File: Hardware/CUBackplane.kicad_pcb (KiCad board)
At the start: 2 copper layers, 84.6 x 83.8 mm, 50 parts, among them CON1 EXPANSION BUS, CON2 EXPANSION BUS, CON3 EXPANSION BUS, CON4 EXPANSION BUS, J1 +5V, J2 -12V, J3 +12V, J4 -5V, J5 +15V, J6 -15V, J7 GND

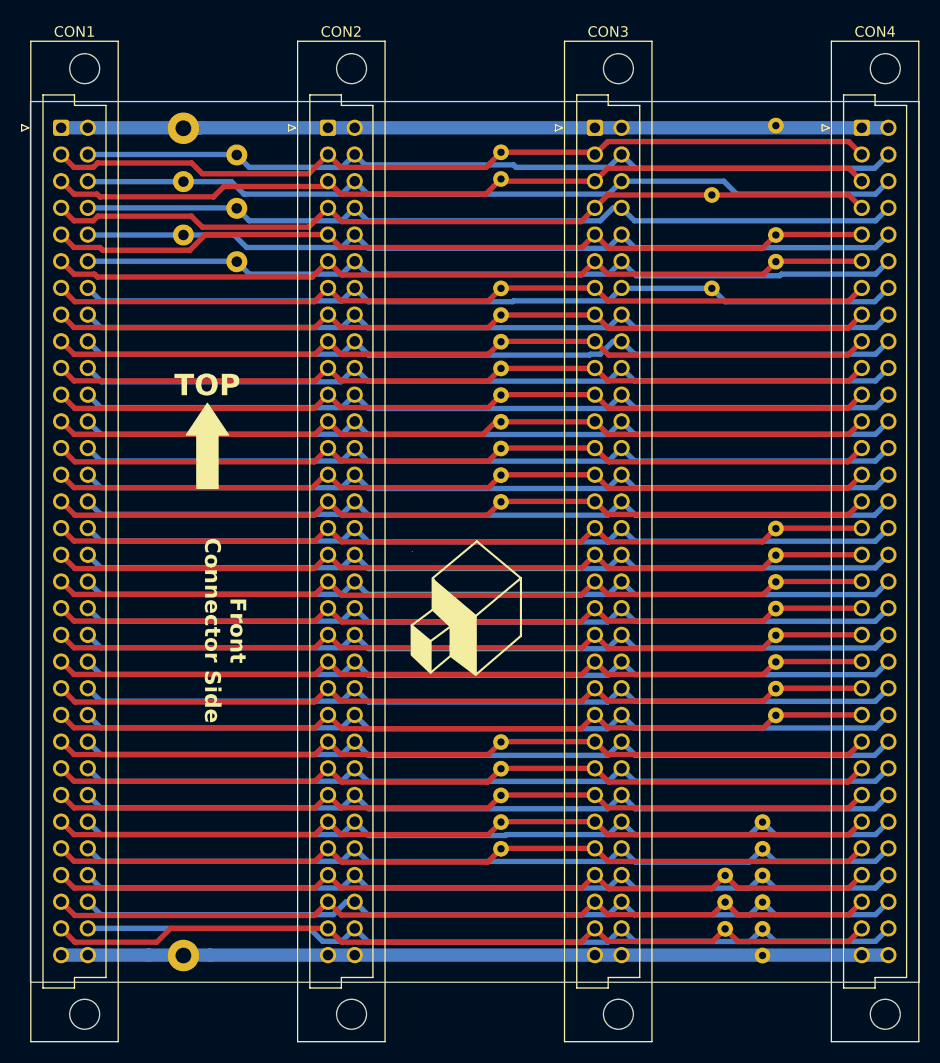
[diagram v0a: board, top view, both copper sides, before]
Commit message: Corrected board outline to 3.3x3.3
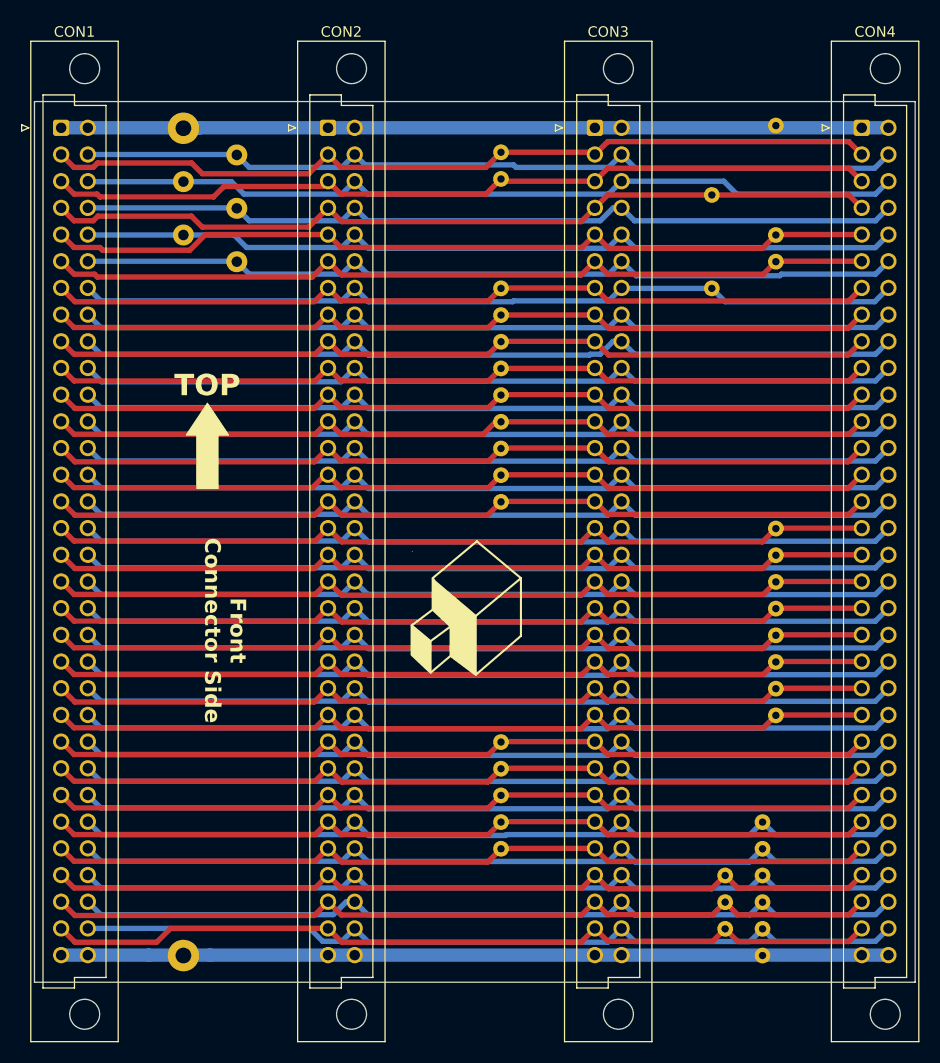
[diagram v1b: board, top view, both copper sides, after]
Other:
- board size 84.6 x 83.8 mm -> 83.8 x 83.8 mm
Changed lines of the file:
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@@
 	)
 	(gr_rect
-		(start 26.8478 34.798)
-		(end 111.4298 118.618)
+		(start 27.224 34.798)
+		(end 111.044 118.618)
 		(stroke
 			(width 0.05)

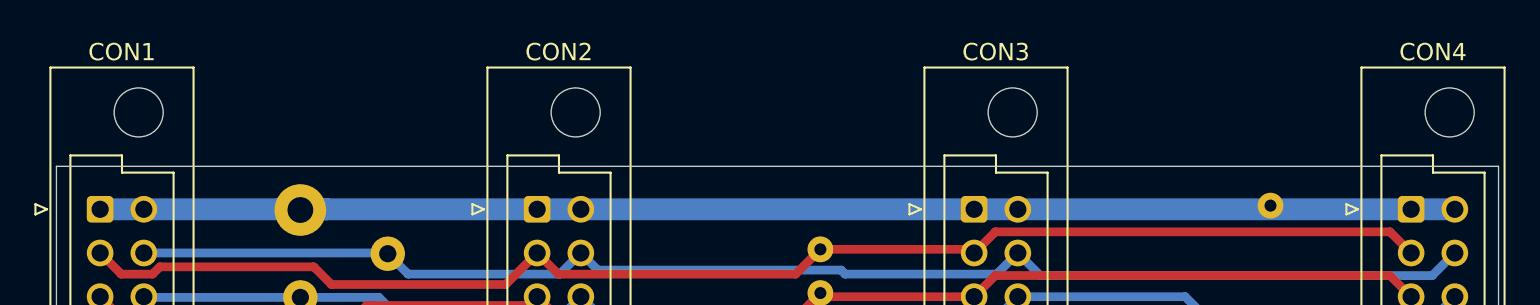
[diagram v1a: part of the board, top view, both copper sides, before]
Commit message: Moved connector references
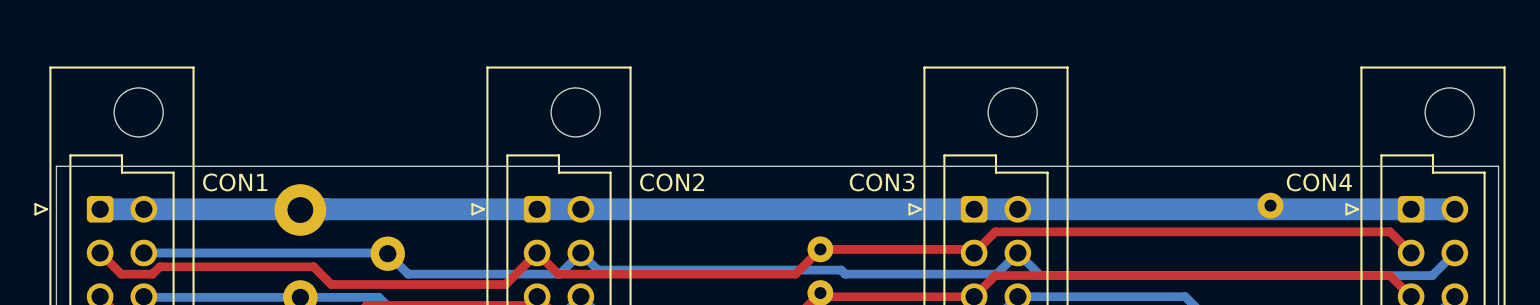
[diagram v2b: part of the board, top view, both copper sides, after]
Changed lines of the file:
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@@
 		(tags "DIN 41612 IEC 60603 B")
 		(property "Reference" "CON2"
-			(at 1.27 -9.13 0)
+			(at 7.874 -1.524 0)
 			(layer "F.SilkS")
 			(effects
@@
 		(tags "DIN 41612 IEC 60603 B")
 		(property "Reference" "CON4"
-			(at 1.27 -9.13 0)
+			(at -5.334 -1.524 0)
 			(layer "F.SilkS")
 			(effects
@@
 		(tags "DIN 41612 IEC 60603 B")
 		(property "Reference" "CON3"
-			(at 1.27 -9.13 0)
+			(at -5.334 -1.524 0)
 			(layer "F.SilkS")
 			(effects
@@
 		(tags "DIN 41612 IEC 60603 B")
 		(property "Reference" "CON1"
-			(at 1.27 -9.13 0)
+			(at 7.874 -1.524 0)
 			(layer "F.SilkS")
 			(effects
